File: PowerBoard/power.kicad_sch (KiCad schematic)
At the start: 21 parts, among them U3 NCV1117DT33T5G, U6 LTC4151IMS_PBF

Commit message: auto discharge circuit
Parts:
- added TP1: GND, bots:TestPoint_Pad_2.0x2.0mm, symbol Connector:TestPoint
- added TP1: SDA, bots:TestPoint_Pad_1.0x1.0mm, symbol Connector:TestPoint
- added TP1: VCC, bots:TestPoint_Pad_2.0x2.0mm, symbol Connector:TestPoint
- added TP1: 3.3V, bots:TestPoint_Pad_2.0x2.0mm, symbol Connector:TestPoint
- added TP1: PGND, bots:TestPoint_Pad_2.0x2.0mm, symbol Connector:TestPoint
- added TP1: SCL, bots:TestPoint_Pad_1.0x1.0mm, symbol Connector:TestPoint
- H1: value MountingHole_Pad -> CANL; footprint MountingHole:MountingHole_2.7mm_M2.5_DIN965_Pad -> bots:MountingHole_2.7mm_M2.5_DIN965_Pad
- H2: value MountingHole_Pad -> PGND; footprint MountingHole:MountingHole_2.7mm_M2.5_DIN965_Pad -> bots:MountingHole_2.7mm_M2.5_DIN965_Pad
- H3: value MountingHole_Pad -> CANH; footprint MountingHole:MountingHole_2.7mm_M2.5_DIN965_Pad -> bots:MountingHole_2.7mm_M2.5_DIN965_Pad
- H4: value MountingHole_Pad -> VCC; footprint MountingHole:MountingHole_2.7mm_M2.5_DIN965_Pad -> bots:MountingHole_2.7mm_M2.5_DIN965_Pad
- U3: footprint bots:DPAK-3_ONS -> DPAK-3_ONS
- U6: footprint bots:MSOP-10_3x3mm_P0.5mm -> LTC4151IMS_PBF:MSOP-10_MS
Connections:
- net +3.3V: now also TP1.1
- net GND: now also TP1.1
- net GNDPWR: now also H2.1, TP1.1
- net VCC: now also H4.1, TP1.1
- net CANL: now reaches H1.1
- net CANH: now reaches H3.1
- net U6SCL: now reaches R1.2, U6.6 (SCL)
- net U6SCL: now also TP1.1
- net U6SDA: now reaches R1.2, U6.7 (SDAI)
- net U6SDA: now also TP1.1
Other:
- moved on the sheet: C1, D2, H3, H4, NT1, R8, U3

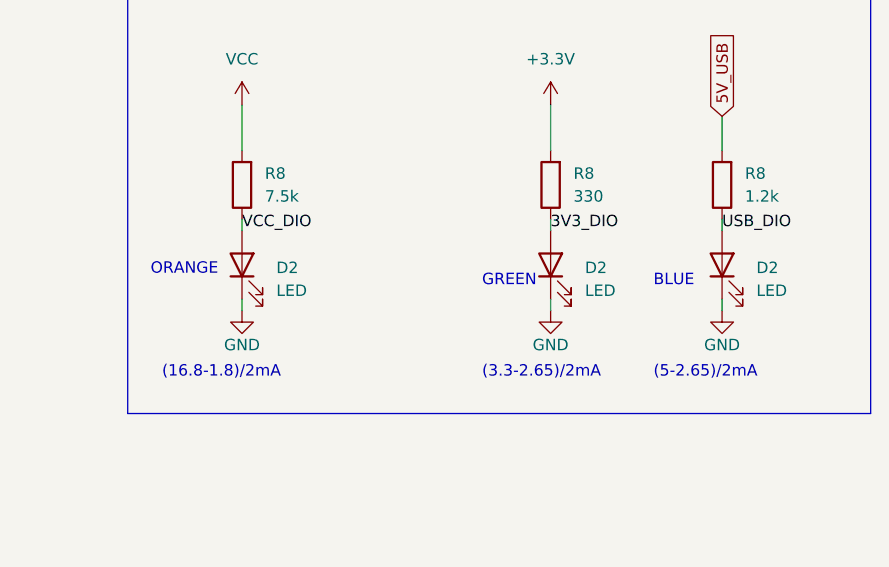
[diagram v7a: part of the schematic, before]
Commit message: updated board edge clearance and cap model
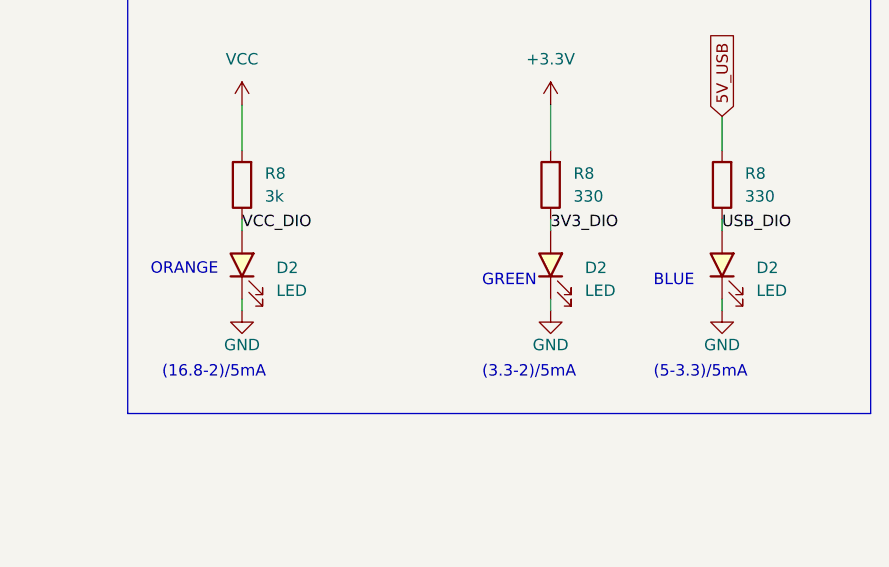
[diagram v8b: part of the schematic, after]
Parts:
- removed R8: 1.2k, bots:R_0603_1608Metric, symbol Device:R
- added R8: 330, bots:R_0603_1608Metric, symbol bots:R_330R
- C1: symbol Device:C -> bots:C_10u; JLC (none) -> 0805; LCSC (none) -> C440198; MPN (none) -> GRM21BR61H106KE43L; Manufacturer (none) -> Murata; Price (none) -> 0.0645
- D2: symbol Device:LED -> bots:LED_green; JLC (none) -> 1206; LCSC (none) -> C264529; MPN (none) -> 23-21/G6C-BL2N1B/2A; Manufacturer (none) -> Everlight Elec; Price (none) -> 0.0488
- D2: footprint bots:LED_1206_3216Metric -> bots:LED_0603_1608Metric; symbol Device:LED -> bots:LED_blue; JLC (none) -> 0603; LCSC (none) -> C2992646; MPN (none) -> 19-21/BHC-AP1Q2/3T; Manufacturer (none) -> Everlight Elec; Price (none) -> 0.0460
- D2: symbol Device:LED -> bots:LED_orange; JLC (none) -> 1206; LCSC (none) -> C712089; MPN (none) -> GBD-C150KFKT-DZ; Manufacturer (none) -> GBG; Price (none) -> 0.0429
- R1: symbol Device:R -> bots:R_5.1k; JLC (none) -> 0603; LCSC (none) -> C23186; MPN (none) -> 0603WAF5101T5E; Manufacturer (none) -> UNI-ROYAL(Uniroyal Elec); Price (none) -> 0.0009
- R1: symbol Device:R -> bots:R_200R; JLC (none) -> 0603; LCSC (none) -> C8218; MPN (none) -> 0603WAF2000T5E; Manufacturer (none) -> UNI-ROYAL(Uniroyal Elec); Price (none) -> 0.0009
- R4: symbol Device:R -> bots:R_4m; JLC (none) -> 1206; LCSC (none) -> C429000; MPN (none) -> MA120610FR004MZ; Manufacturer (none) -> Ever Ohms Tech; Price (none) -> 0.0667
- R8: value 7.5k -> 3k; symbol Device:R -> bots:R_7.5k; JLC (none) -> 0603; LCSC (none) -> C23234; MPN (none) -> 0603WAF7501T5E; Manufacturer (none) -> UNI-ROYAL(Uniroyal Elec); Price (none) -> 0.0009
- R8: symbol Device:R -> bots:R_330R; JLC (none) -> 0603; LCSC (none) -> C23138; MPN (none) -> 0603WAF3300T5E; Manufacturer (none) -> UNI-ROYAL(Uniroyal Elec); Price (none) -> 0.0009
- TP1: symbol Connector:TestPoint -> bots:TestPoint_2x2; now left out of the parts list
- TP1: symbol Connector:TestPoint -> bots:TestPoint_1x1; now left out of the parts list
- U3: footprint DPAK-3_ONS -> bots:DPAK-3_ONS; JLC (none) -> TO-252; LCSC (none) -> C20625; MPN (none) -> NCV1117DT33T5G; Manufacturer (none) -> onsemi; Price (none) -> 0.5575
- U6: footprint LTC4151IMS_PBF:MSOP-10_MS -> bots:MSOP-10_3x3mm_P0.5mm; Availability In Stock -> (none); Check_prices https://www.snapeda.com/parts/LTC4151IMS%23PBF/Analog+Devic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 -> (none); MANUFACTURER_PART_NUMBER ltc4151ims -> (none); MF Analog Devices -> (none); MP LTC4151IMS#PBF -> (none); MPN (none) -> LTC4151IMS#PBF; Manufacturer (none) -> Analog Devices; Package MSOP-10 Analog Devices -> (none); Price None -> 14.07; Purchase-URL https://www.snapeda.com/api/url_track_click_mouser/?unipart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 -> (none); SnapEDA_Link https://www.snapeda.com/parts/LTC4151IMS%23PBF/Analog+Devic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 -> (none); VENDOR LinearTech -> (none)
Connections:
- net 5V_USB: now also R8.2
- net USB_DIO: now also R8.1
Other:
- note added: "(16.8-2)/5mA"
- note added: "(3.3-2)/5mA"
- note added: "(5-3.3)/5mA"
- note removed: "(16.8-1.8)/2mA"
- note removed: "(3.3-2.65)/2mA"
- note removed: "(5-2.65)/2mA"
